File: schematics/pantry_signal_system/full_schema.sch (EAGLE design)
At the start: 93 parts, among them J1 USBASP_PIN, J2 JST-XH254-3P, J3 JST-XH254-2P, J4 JST-XH254-2P, J5 JST-XH254-3P, J6 JST-XH254-2P, J7 JST-XH254-2P, J8 JST-XH254-2P, J9 JST-XH254-2P, Q1 FDS4935A, Q2 FDS4935A, Q3 FDS4935A, Q4 STP14NM50N, Q5 2N3904, Q6 STP14NM50N, Q7 STP14NM50N, SW1 SWITCH, SW2 SWITCH, U1 NC7WZ04, U10 FAN73611, U11 ATMEGA328P, U12 E220-900T22D, U13 BME280BME280-CONNECTOR-ONLY, U14 2004A I2C, U2 AD8544, U3 FAN73611, U4 FAN73611, U5 MCP1703T-5002E/CB, U6 MCP1703T-5002E/CB, U7 MCP1703T-3302E/CB, U8 FAN73611, U9 ATTINY13

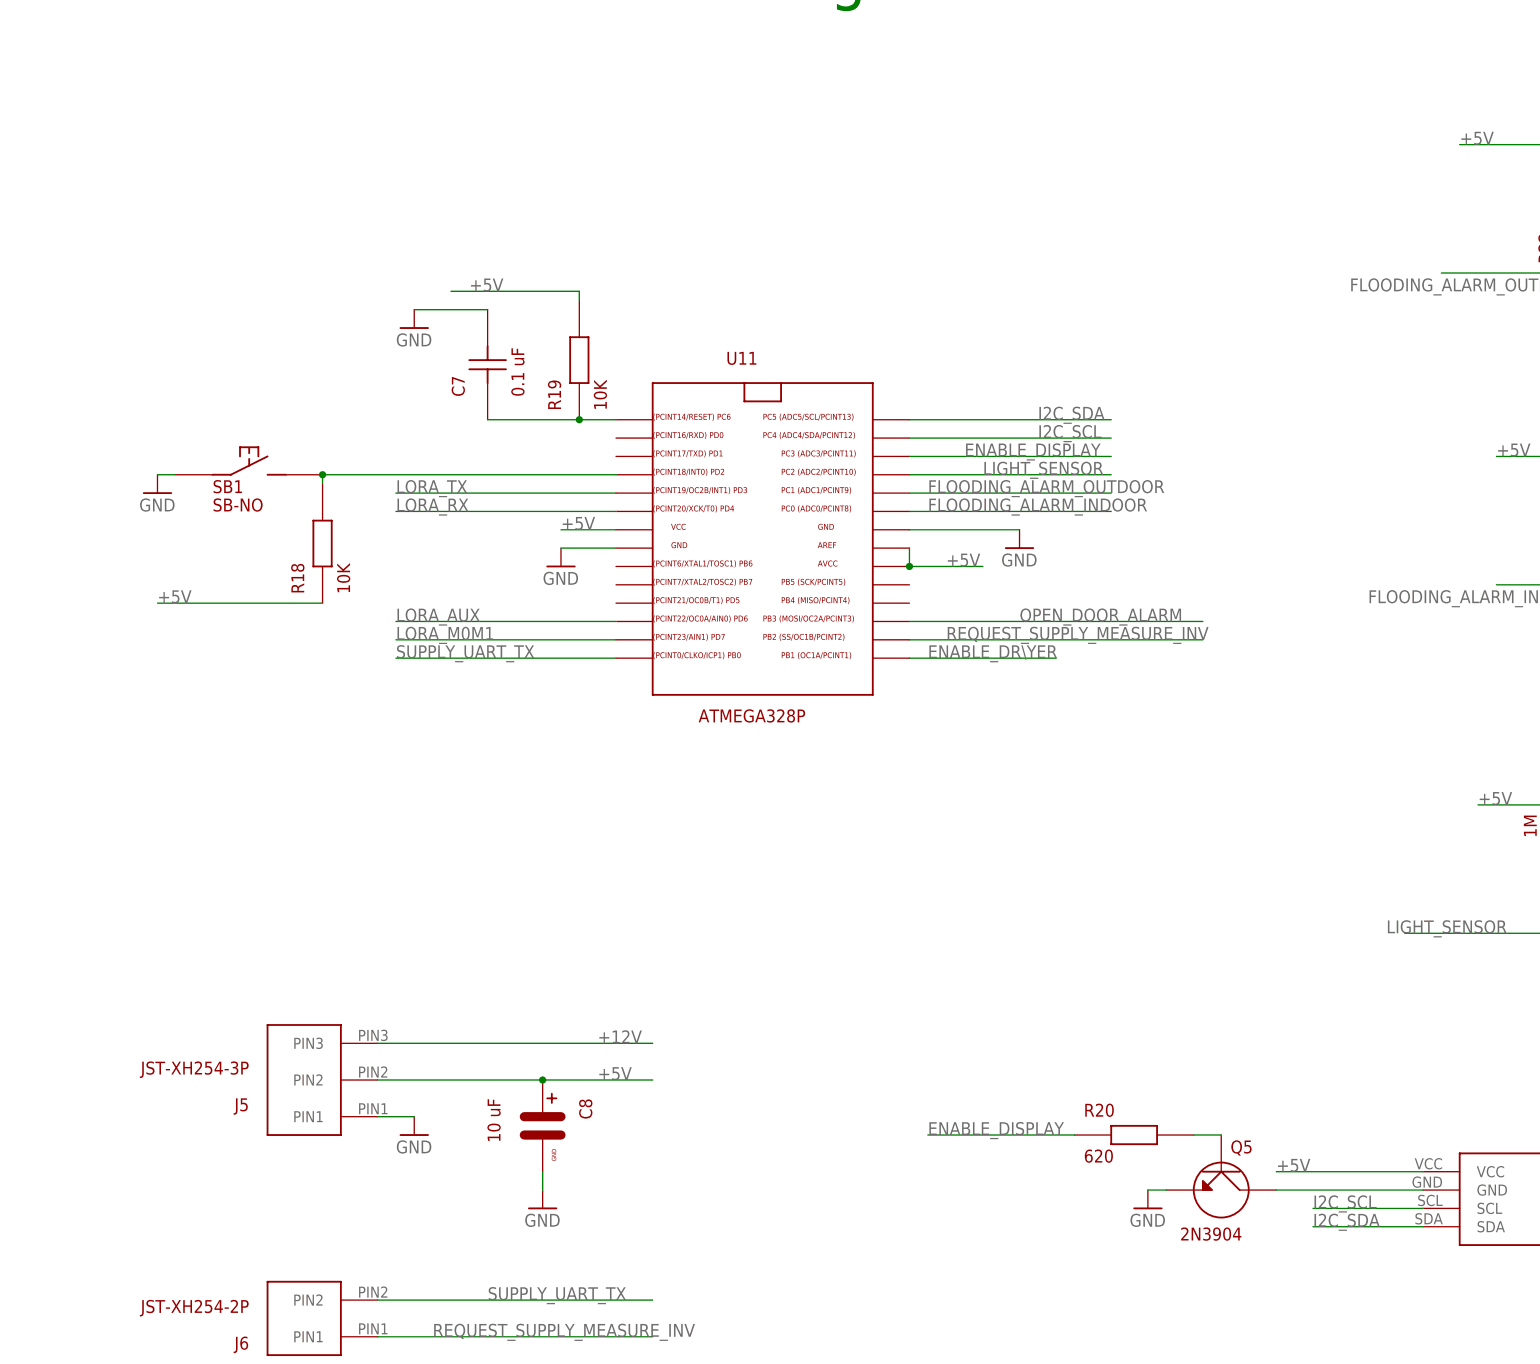
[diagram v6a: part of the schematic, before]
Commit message: Try to fix problem with I2C bus and display module
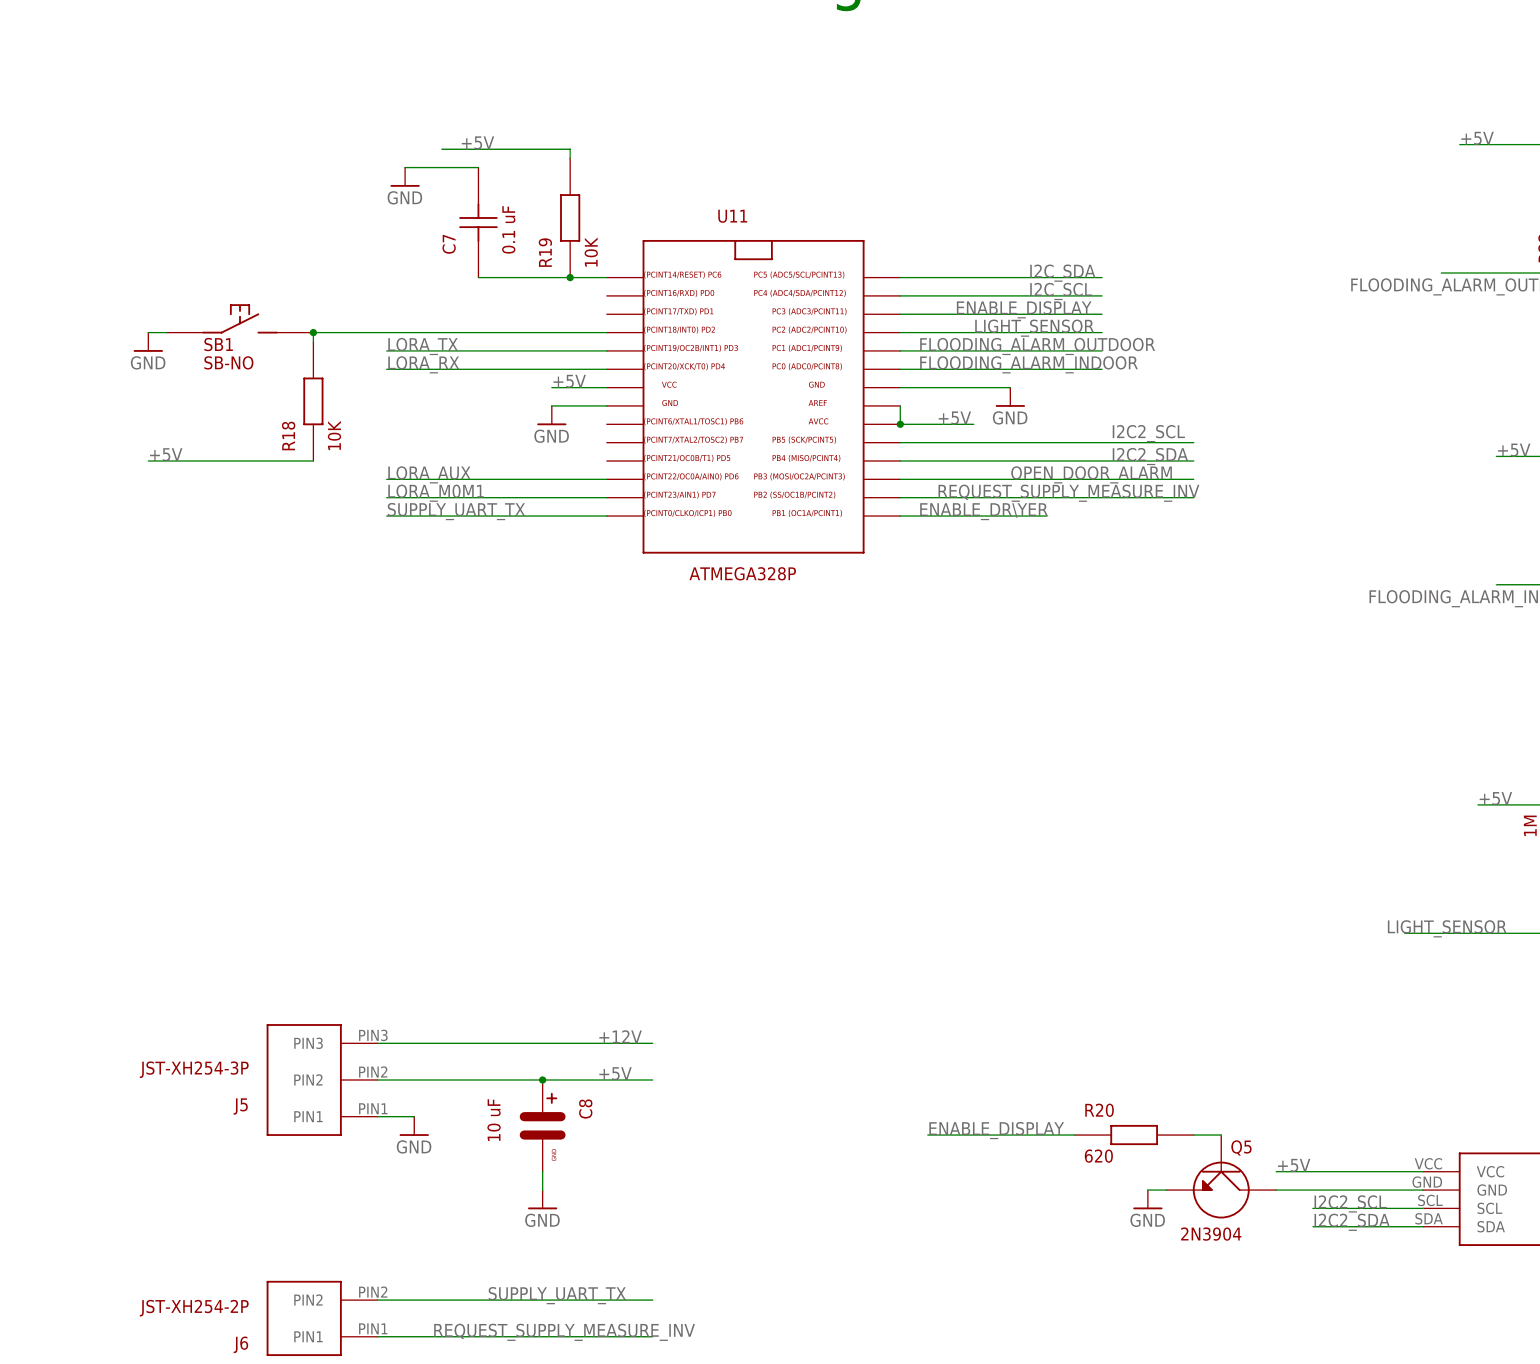
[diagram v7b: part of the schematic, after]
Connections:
- new net I2C2_SCL: U11.PB5, U14.SCL
- new net I2C2_SDA: U11.PB4, U14.SDA
- net I2C_SCL: no longer U14.SCL
- net I2C_SDA: no longer U14.SDA
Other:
- moved on the sheet: C7, R18, R19, SB1, U11
